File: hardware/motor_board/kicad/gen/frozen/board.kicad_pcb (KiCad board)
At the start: 6 copper layers, 75 x 35 mm, 237 parts, among them J1 BOOMELE_1.27-2x10P, J2 WAFER-SH1.0-6PWB, J3 WAFER-SH1.0-6PWB, J4 S5B-XH-A, Q1 HYG015N04LS1C2, Q2 HYG015N04LS1C2, Q3 HYG015N04LS1C2, Q4 HYG015N04LS1C2, Q5 HYG015N04LS1C2, Q6 HYG015N04LS1C2, Q7 HYG015N04LS1C2, Q8 HYG015N04LS1C2, U1 STM32G474RET6, U10 SN74LVC3G17DCUR, U11 TPS22945DCKR, U12 TPS22945DCKR, U13 LM74502DDFR, U14 74LVC1G17SE-7, U2 DRV8323RHRGZR, U3 DRV8316CRRGFR, U4 DRV8316CRRGFR, U5 AP2112K-3.3TRG1, U6 SN74LVC08APWR, U7 INA239AIDGSR, U8 BQ76907RGRR, U9 SN74LVC3G17DCUR

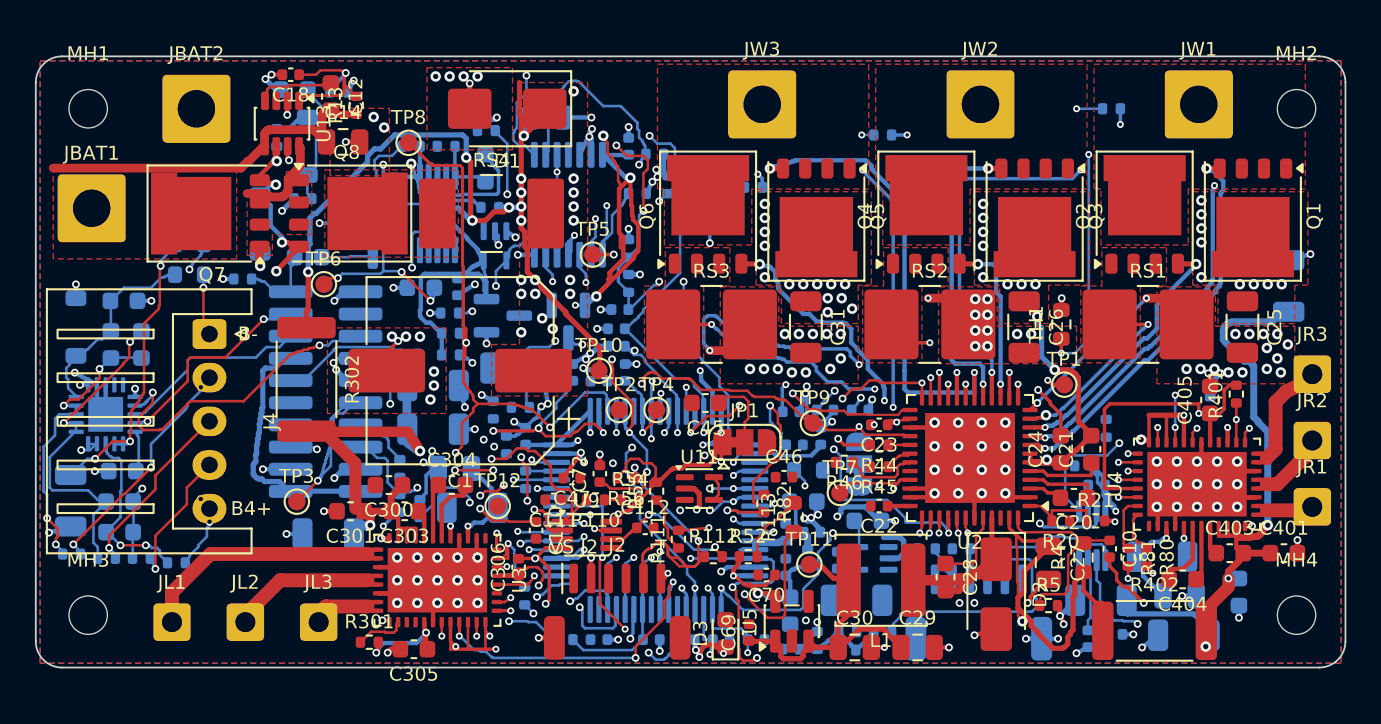
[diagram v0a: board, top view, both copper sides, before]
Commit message: tail: own GND drop via for fill-only GND pads (fillonly.py; ~63 placed), islands.py, plot.py; DRC 0, 75 open
Co-Authored-By: Claude Opus 5.5 (1M context) <noreply@anthropic.com>
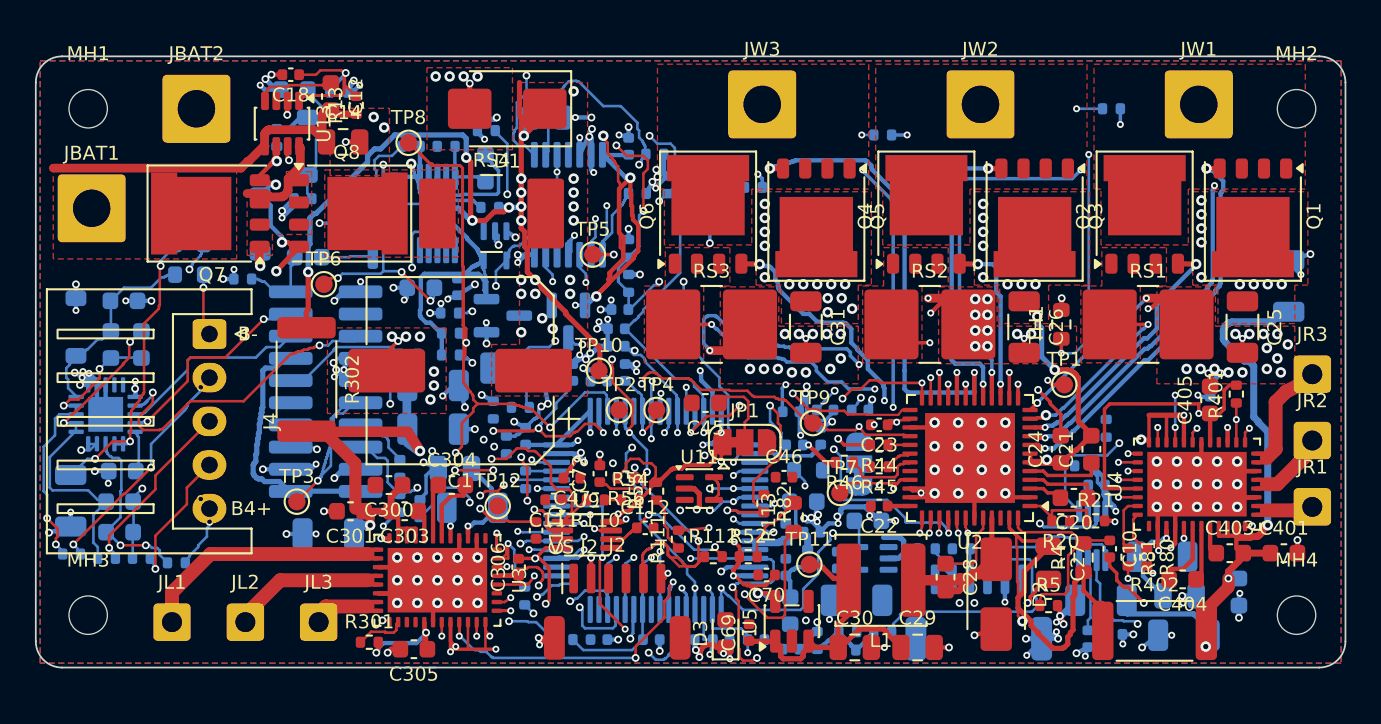
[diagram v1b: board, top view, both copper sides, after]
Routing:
- net GND: track 155.1 -> 217.2 mm, vias 203 -> 266
- net +3V3: track 168.1 -> 171.7 mm, vias 24 -> 27

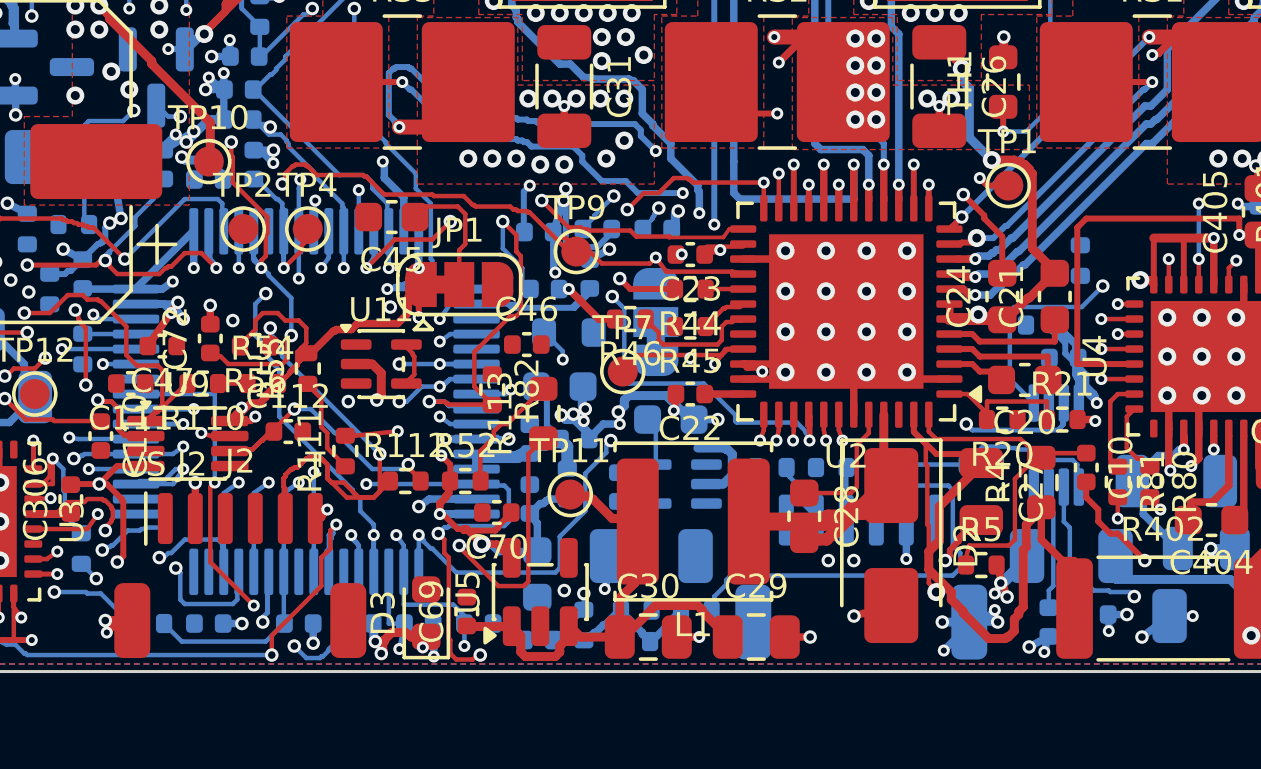
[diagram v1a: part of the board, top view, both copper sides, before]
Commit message: tail: right-sensor set re-routed together, via-in-pad op (filled+capped per FAB.md) for 3 boxed-in pads; DRC 0, 73 open
Co-Authored-By: Claude Opus 5.5 (1M context) <noreply@anthropic.com>
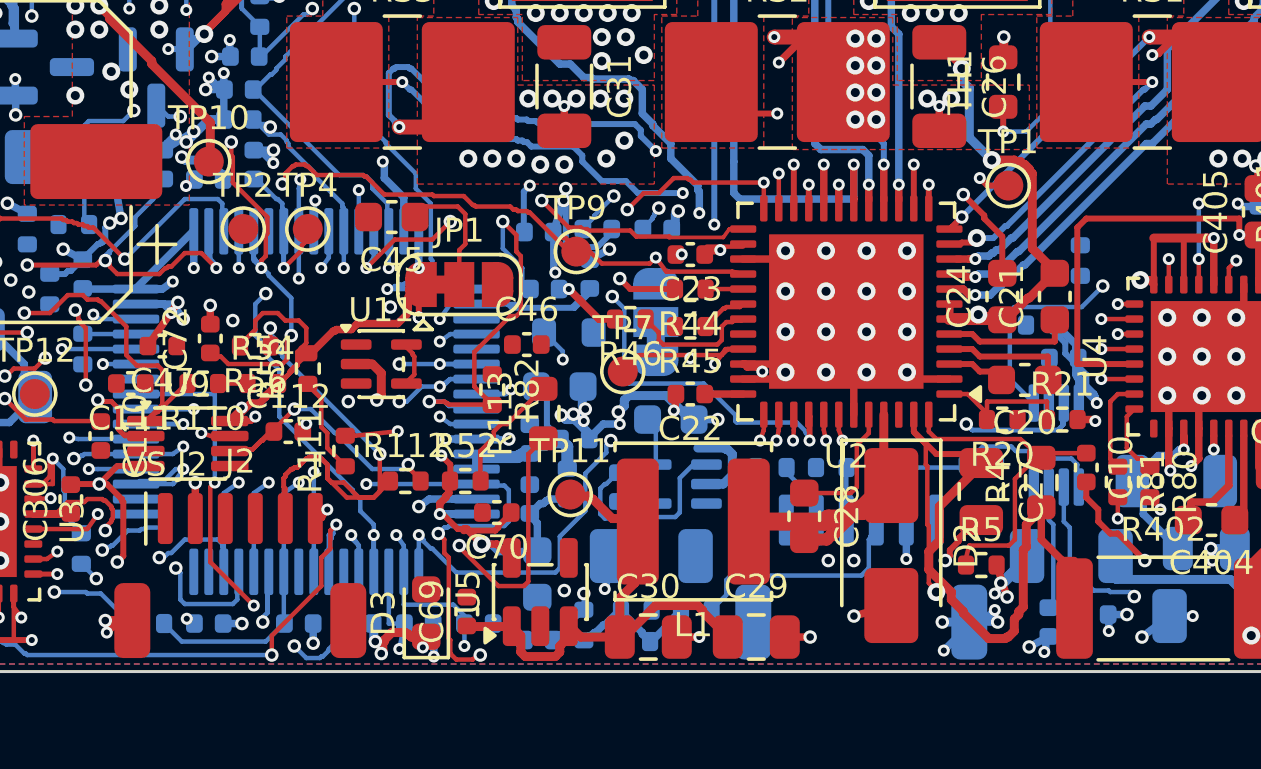
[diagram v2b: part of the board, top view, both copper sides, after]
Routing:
- net /sensors/R_H1: track 17.0 -> 9.57 mm
- net /sensors/R_VS: track 0.00 -> 6.68 mm
- net GND: vias 266 -> 267
- net +3V3: vias 27 -> 29

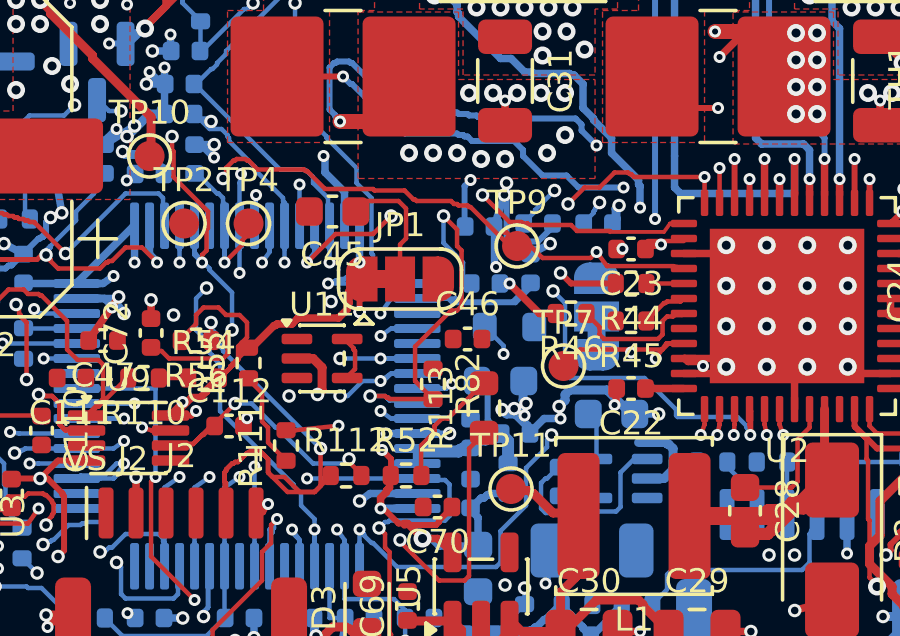
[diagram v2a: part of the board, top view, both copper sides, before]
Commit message: tail: C92 to F under R82 (R_SOC_F loop gone), U1.19 W_VB to C42; spot.py SPOT_GEOM/SPOT_PADSONLY; DRC 0, 72 open
Co-Authored-By: Claude Opus 5.5 (1M context) <noreply@anthropic.com>
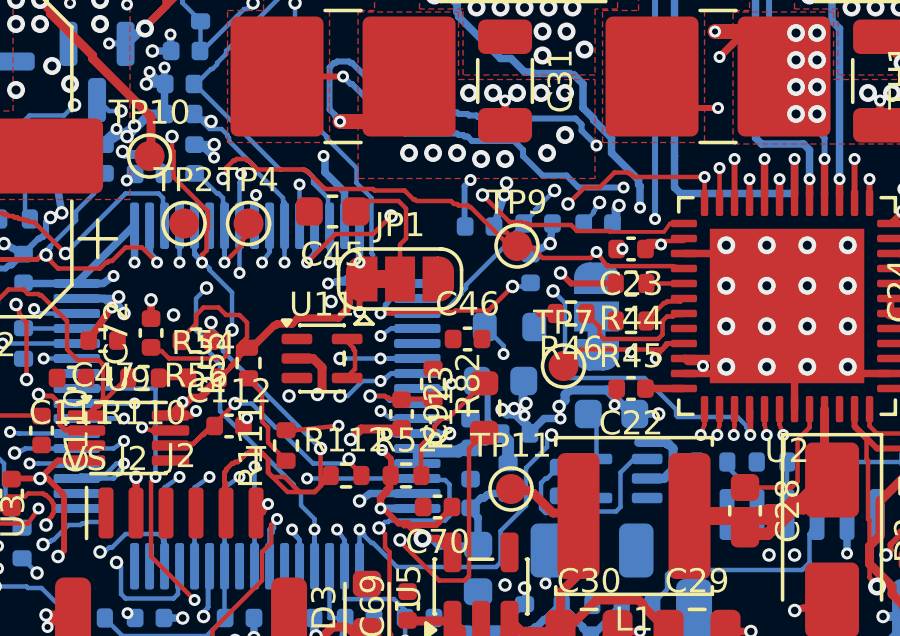
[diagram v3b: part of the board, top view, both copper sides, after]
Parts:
- C92: moved to F.Cu
- moved C92 5.17 mm to (140.7, 96.6), turned to -90 degrees
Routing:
- net /mcu/R_SOC_F: track 13.9 -> 5.01 mm, vias 2 -> 1
- net W_VB: track 17.9 -> 22.8 mm
- net GND: track 217.2 -> 213.3 mm, vias 267 -> 266
- net W_VA: track 11.3 -> 9.91 mm, vias 2 -> 3
